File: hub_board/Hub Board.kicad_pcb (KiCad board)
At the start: 4 copper layers, 42.5 x 38.5 mm, 26 parts, among them J1 DotStar, J2 DotStar, J3 DotStar, J4 DotStar, J5 Sensor, P4 SERIAL, SW1 Switch_SPDT_x2, SW2 Switch_DPST, U0 10118194, U1 LM3671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

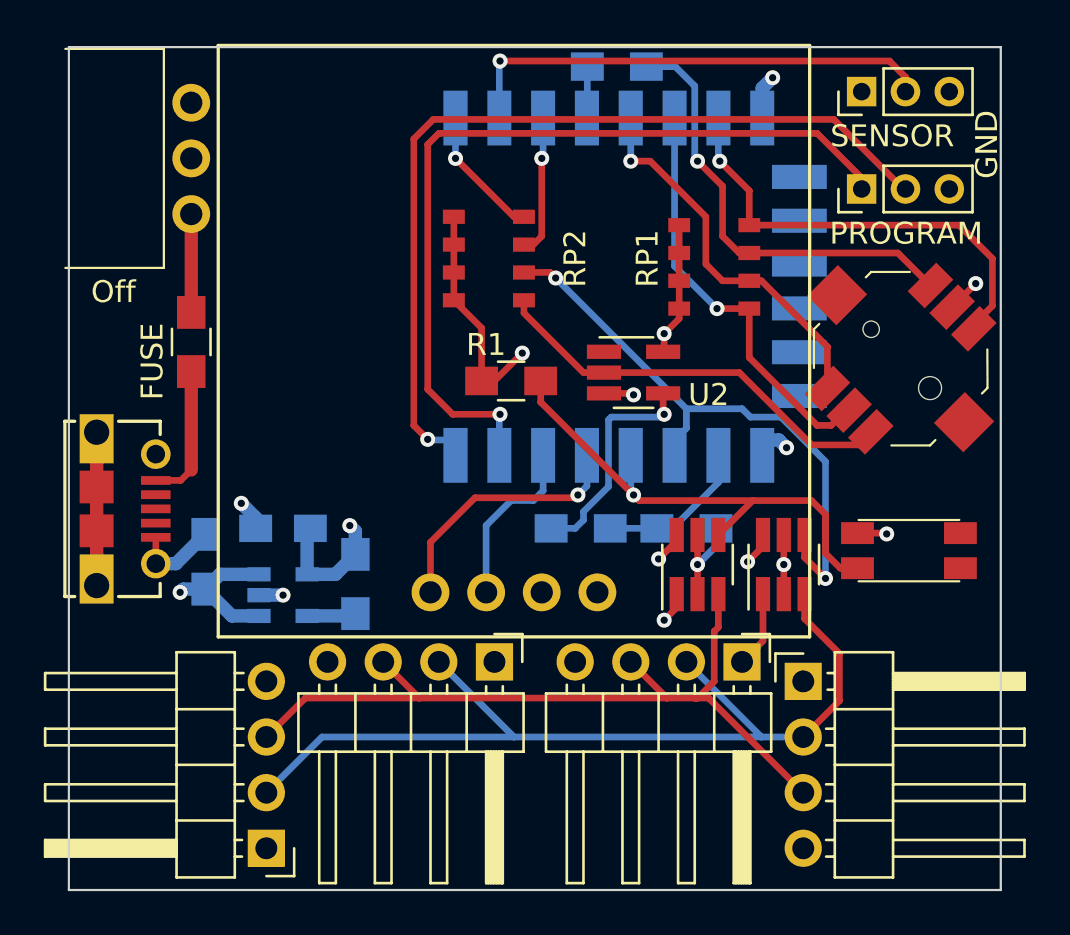
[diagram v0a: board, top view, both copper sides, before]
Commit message: Finished redesigning for WS2812B LEDs
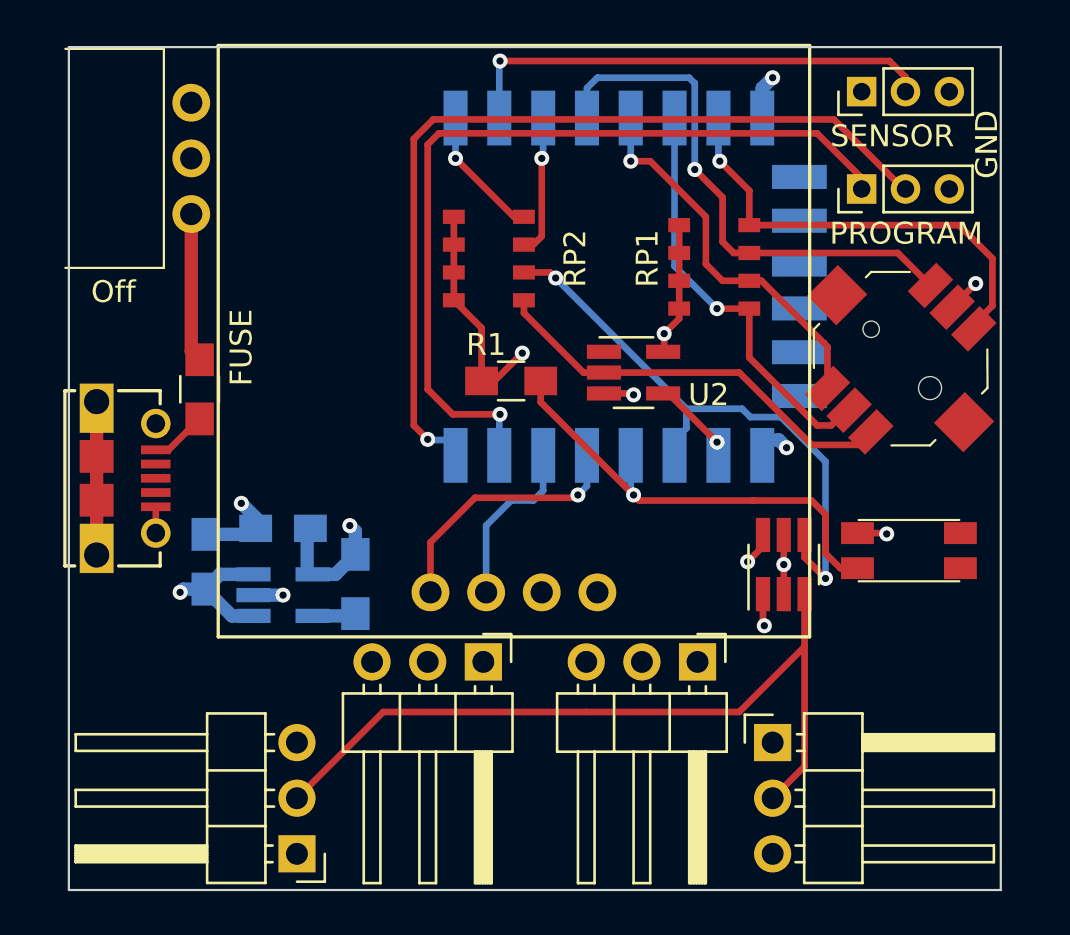
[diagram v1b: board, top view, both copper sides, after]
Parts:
- removed R4: 10k, Resistors_SMD:R_0805_HandSoldering
- removed R7, R8: 0, Resistors_SMD:R_0805_HandSoldering
- removed U6: SN74LVC1T45 - MOSI, TO_SOT_Packages_SMD:SOT-23-6_Handsoldering
- J1, J2, J3, J4: value DotStar -> NeoPixel; footprint Pin_Headers:Pin_Header_Angled_1x04_Pitch2.54mm -> Pin_Headers:Pin_Header_Angled_1x03_Pitch2.54mm
- U1: footprint TO_SOT_Packages_SMD:SOT-23-5 -> TO_SOT_Packages_SMD:SOT-23-5_HandSoldering
- U7: value SN74LVC1T45 - SCLK -> SN74LVC1T45
- moved J3 3.12 mm to (126.1, 134.9)
- moved F0 2.19 mm to (99.9, 118.8)
- moved J4 2.03 mm to (122.6, 131.2)
- moved J1 1.42 mm to (104.3, 140.0)
- moved U0 1.40 mm to (95.2, 122.8)
- moved J2 0.51 mm to (112.8, 131.2)
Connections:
- J1 pad 1: +5V -> GND
- J1 pad 3: Net-(J1-Pad3) -> +5V
- J2 pad 1: +5V -> GND
- J2 pad 3: Net-(J1-Pad3) -> +5V
- J3 pad 1: +5V -> GND
- J3 pad 3: Net-(J1-Pad3) -> +5V
- J4 pad 1: +5V -> GND
- J4 pad 3: Net-(J1-Pad3) -> +5V
- RP1 pad 3: Net-(R8-Pad2) -> Net-(RP1-Pad3)
- U2 pad 4: Net-(R7-Pad1) -> Net-(U2-Pad4)
- U3 pad 10: Net-(R4-Pad1) -> Net-(U2-Pad4)
- U3 pad 4: Net-(R8-Pad1) -> Net-(RP1-Pad3)
- U5 pad 4: Net-(R8-Pad2) -> Net-(RP1-Pad3)
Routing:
- net Net-(J1-Pad3): track 37.0 -> 0.00 mm
- net Net-(RP1-Pad3): track 0.00 -> 25.7 mm, vias 0 -> 1
- net Net-(R8-Pad2): track 20.7 -> 0.00 mm, vias 1 -> 0
- net Net-(R7-Pad1): track 10.3 -> 0.00 mm, vias 1 -> 0
- net Net-(R4-Pad1): track 7.74 -> 0.00 mm
- net Net-(J1-Pad2): track 43.1 -> 36.0 mm
- net GND: track 28.0 -> 21.3 mm, vias 8 -> 7
- net Net-(F0-Pad2): track 6.31 -> 2.58 mm
- net Net-(U2-Pad4): track 0.00 -> 3.50 mm, vias 0 -> 1
- net +5V: track 11.8 -> 8.37 mm
- net Net-(R8-Pad1): track 3.05 -> 0.00 mm
- net Net-(F0-Pad1): track 4.49 -> 6.81 mm
- net Net-(R1-Pad2): track 24.4 -> 22.2 mm
- net VCC: track 28.3 -> 26.9 mm, vias 6 -> 5
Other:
- board text added: "Raver Lights Hub v3.3 Copyright Bryan Hughes 2018"
- board text removed: "Raver Lights Hub v3.2 Copyright Bryan Hughes 2018"

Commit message: Finished layout
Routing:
- net Net-(J1-Pad2): track 36.0 -> 42.3 mm
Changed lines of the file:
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@@
   (general
     (links 75)
-    (no_connects 4)
-    (area 93.869999 103.109999 136.515001 141.691001)
+    (no_connects 0)
+    (area 89.4366 102.182837 141.57021 143.2874)
     (thickness 1.6)
     (drawings 10)
-    (tracks 209)
+    (tracks 213)
     (zones 0)
     (modules 22)
@@
   (segment (start 102.599 127.229) (end 100.819 127.229) (width 0.6096) (layer B.Cu) (net 5))
   (segment (start 100.819 127.229) (end 100.143 127.905) (width 0.6096) (layer B.Cu) (net 5))
-  (segment (start 117.542 133.513) (end 124.527 133.513) (width 0.3048) (layer F.Cu) (net 6))
+  (segment (start 120.082 131.227) (end 120.082 131.354) (width 0.3048) (layer F.Cu) (net 6))
+  (segment (start 120.082 131.354) (end 117.923 133.513) (width 0.3048) (layer F.Cu) (net 6))
+  (segment (start 108.271 133.513) (end 117.923 133.513) (width 0.3048) (layer F.Cu) (net 6))
+  (segment (start 117.923 133.513) (end 124.527 133.513) (width 0.3048) (layer F.Cu) (net 6))
   (segment (start 124.527 133.513) (end 127.509 130.531) (width 0.3048) (layer F.Cu) (net 6))
-  (segment (start 108.271 133.513) (end 117.542 133.513) (width 0.3048) (layer F.Cu) (net 6))
+  (segment (start 110.303 131.227) (end 110.303 131.481) (width 0.3048) (layer F.Cu) (net 6))
+  (segment (start 110.303 131.481) (end 108.271 133.513) (width 0.3048) (layer F.Cu) (net 6))
   (segment (start 104.334 137.45) (end 108.271 133.513) (width 0.3048) (layer F.Cu) (net 6))
   (segment (start 127.509 128.132) (end 127.509 130.531) (width 0.3048) (layer F.Cu) (net 6))
